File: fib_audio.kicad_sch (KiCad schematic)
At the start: 58 parts, among them J701 DNP AUDIO-JACK-8P-SMD, J702 SPK_JST_L, J703 SPK_JST_R, K701 BUTTON-4PDTSM-62K-S-V-T/R(SN4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, U701 WM8960CGEFL, X701 24MHz 306020014

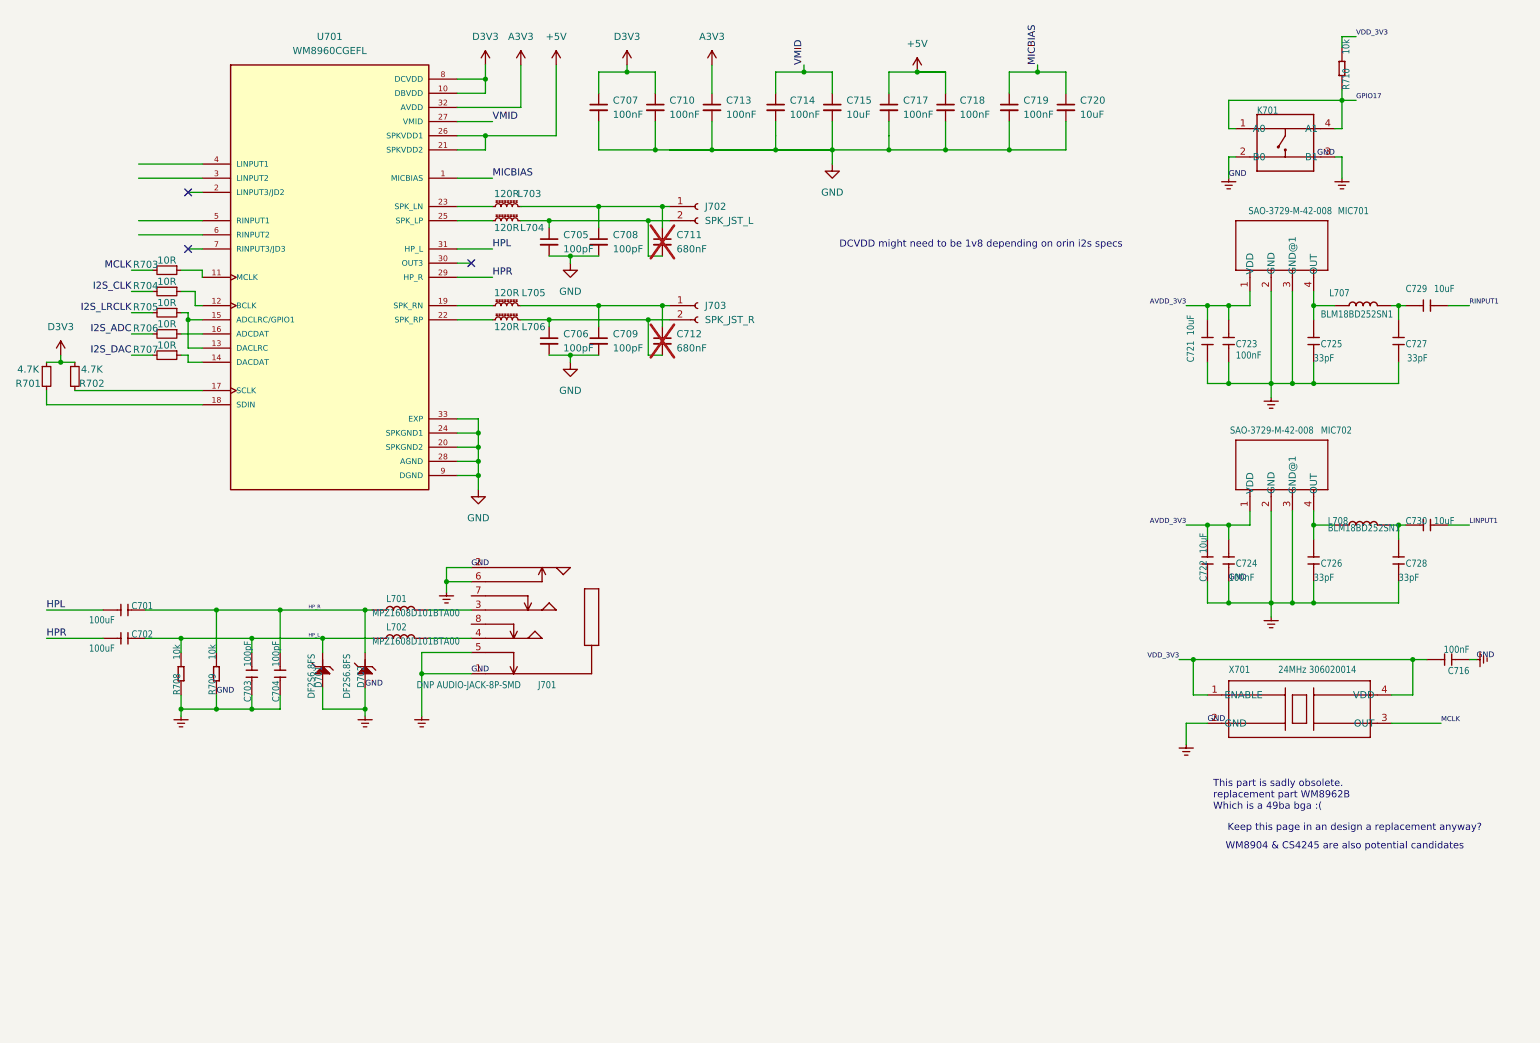
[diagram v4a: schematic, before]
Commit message: added all missing footprints, fixed library & footprint links, did layout out 99% of components, all that's left is rtc(?), peripherals, routing & lengthmatching and final sanity checks
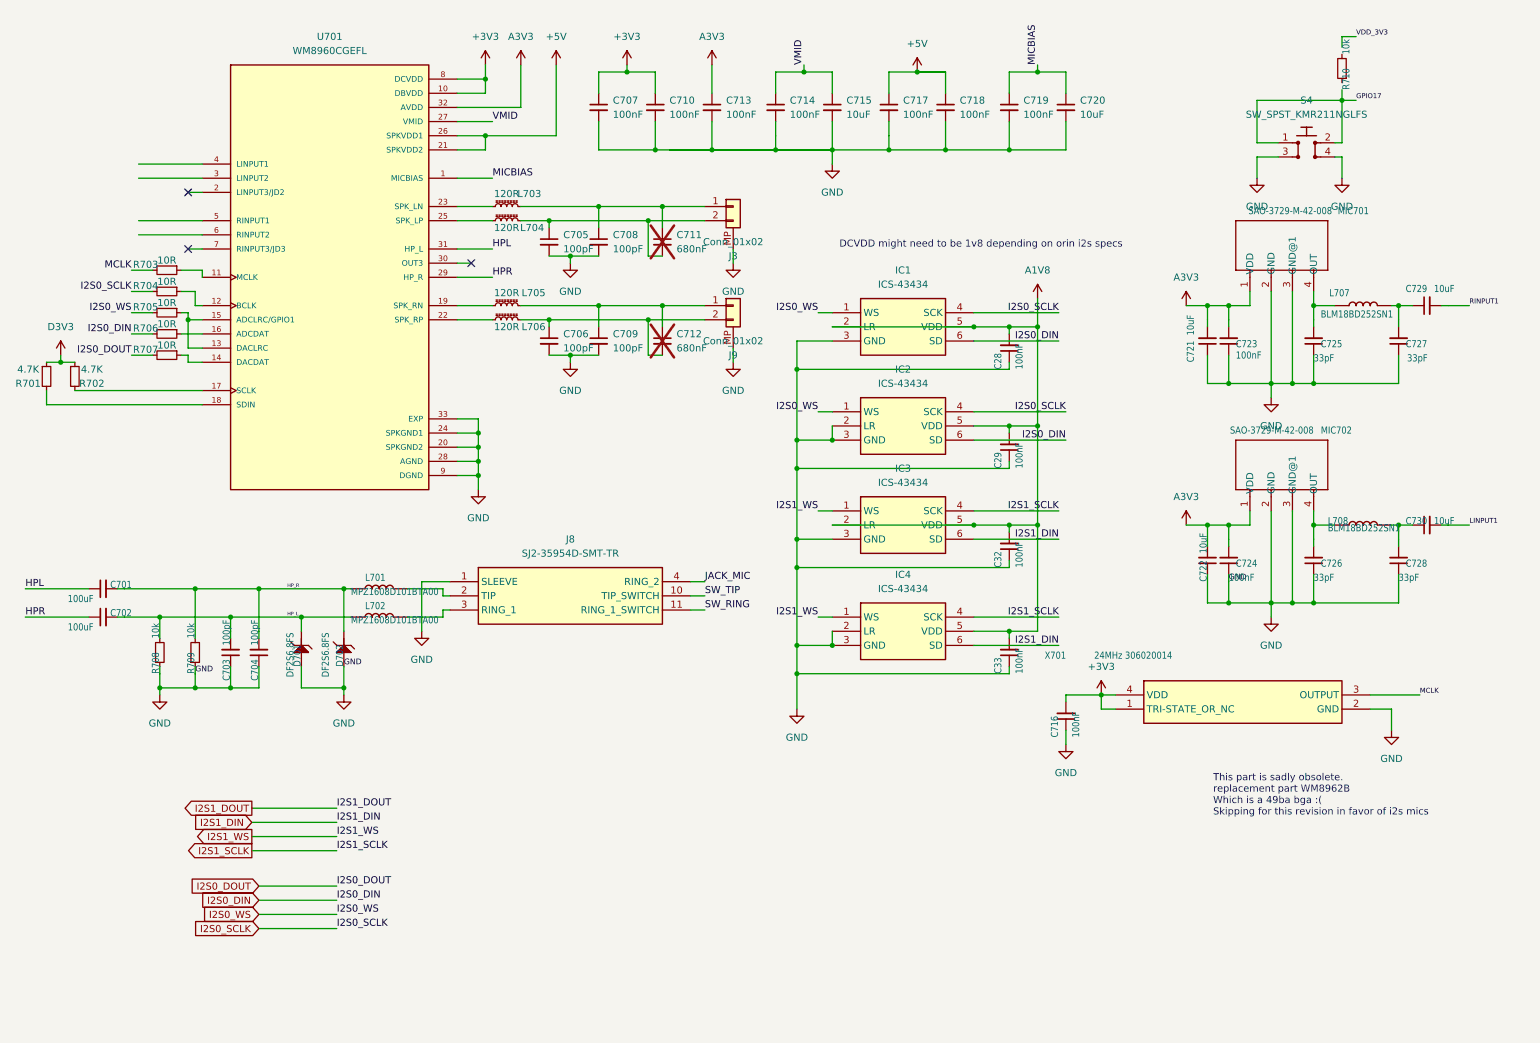
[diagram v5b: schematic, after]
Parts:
- removed J701: DNP AUDIO-JACK-8P-SMD, Untitled:AUDIO8P-SMD-3.5-14.5X6.1X4.0MM, symbol Untitled-eagle-import:AUDIO-JACK-8P-SMD'PJ-393'
- removed J702: SPK_JST_L, Capacitor_SMD:C_0603_1608Metric, symbol Connector:Conn_01x02_Socket
- removed J703: SPK_JST_R, Capacitor_SMD:C_0603_1608Metric, symbol Connector:Conn_01x02_Socket
- removed K701: BUTTON-4PDTSM-62K-S-V-T/R(SN431), Untitled:SW4-SMD-6.0X6.0X5.0MM, symbol Untitled-eagle-import:BUTTON-4PDTSM-62K-S-V-T/R(SN431)
- added C28, C29, C32, C33: 100nF, Capacitor_SMD:C_0402_1005Metric, symbol Fibel2:C_Small_Rota
- added IC1, IC2, IC3, IC4: ICS-43434, ICS43434, symbol Fibel2:ICS-43434
- added J3, J9: Conn_01x02, Connector_JST:JST_PH_S2B-PH-SM4-TB_1x02-1MP_P2.00mm_Horizontal, symbol Fibel2:JST_2_SMD
- added J8: SJ2-35954D-SMT-TR, SJ235954DSMTTR, symbol Fibel2:SJ2-35954D-SMT-TR
- added S4: SW_SPST_KMR211NGLFS, Fibel2:KMR211NGLFS, symbol Fibel2:SW_KMR211NGLFS_SMD
- C701, C702: symbol Untitled-eagle-import:CAP-0805 -> Fibel2:C_Small_Rota
- C703, C704, C716, C723, C724, C725, C726, C727, C728: symbol Untitled-eagle-import:CAP-0402 -> Fibel2:C_Small_Rota
- C721, C722, C729, C730: symbol Untitled-eagle-import:CAP-0603 -> Fibel2:C_Small_Rota
- D701, D702: symbol Untitled-eagle-import:D-ESD-2P'DF2S6.8FS' -> Fibel2:D-ESD-2P'DF2S6.8FS'
- L701, L702, L707, L708: symbol Untitled-eagle-import:INDUCTOR/FERRITE-BEAD'0603' -> Fibel2:INDUCTOR/FERRITE-BEAD'0603'
- MIC701, MIC702: footprint Untitled:MIC4-SMD-3.76X2.95MM -> Fibel2:MIC_Respeaker; symbol Untitled-eagle-import:MIC-MSM421A3729H8-C -> Fibel2:MIC-MSM421A3729H8-C
- R708, R709, R710: symbol Untitled-eagle-import:Discrete-new_RES-0402 -> Fibel2:R_Small_Rota
- X701: footprint Untitled:OSC4-SMD-2.5X2.0X0.8MM -> Fibel2:ECS2520MV; symbol Untitled-eagle-import:CRYSTAL-OSCILLATOR2.52.0 -> Fibel2:ECS-327ATQ2520MV-24M; Height (none) -> 0.9; Manufacturer_Name (none) -> ECS; Manufacturer_Part_Number (none) -> ECS-327ATQ2520MV-BS-TR; Mouser Part Number (none) -> 520-327ATQ2520MVBSTR; Mouser Price/Stock (none) -> https://www.mouser.co.uk/ProductDetail/ECS/ECS-327ATQ2520MV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
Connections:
- net AVDD_3V3 is gone; now on net A3V3: C721.2, C722.2, C723.2, C724.2, MIC701.1 (VDD), MIC702.1 (VDD)
- net D3V3: no longer C707.1, C710.1, U701.10 (DBVDD), U701.8 (DCVDD)
- net GND: now also C28.1, C29.1, C32.1, C33.1, IC1.3 (GND), IC2.2 (LR), IC2.3 (GND), IC3.3 (GND), IC4.2 (LR), IC4.3 (GND), J3.MP, J8.1 (SLEEVE), J9.MP, S4.3, S4.4
- net GPIO17: now also S4.1, S4.2; no longer R710.1
- net VDD_3V3: no longer C716.2, R710.2, X701.1 (ENABLE), X701.4 (VDD)
- net at C709.1, C712.1, L705.2: now also J9.1 (Pin_1)
- net at C706.1, C712.2, L706.2: now also J9.2 (Pin_2)
- net at C705.1, C711.2, L704.2: now also J3.2 (Pin_2)
- net at L701.2: now also J8.2 (TIP)
- net at L702.2: now also J8.3 (RING_1)
- net at C708.1, C711.1, L703.2: now also J3.1 (Pin_1)
- net I2S_ADC renamed I2S0_DIN
- net I2S0_DIN: now also IC1.6 (SD), IC2.6 (SD)
- net I2S_CLK renamed I2S0_SCLK
- net I2S0_SCLK: now also IC1.4 (SCK), IC2.4 (SCK)
- net I2S_DAC renamed I2S0_DOUT
- net I2S_LRCLK renamed I2S0_WS
- net I2S0_WS: now also IC1.1 (WS), IC2.1 (WS)
- new net +3V3: C707.1, C710.1, C716.2, U701.10 (DBVDD), U701.8 (DCVDD), X701.1 (TRI-STATE_OR_NC), X701.4 (VDD)
- new net A1V8: C28.2, C29.2, C32.2, C33.2, IC1.2 (LR), IC1.5 (VDD), IC2.5 (VDD), IC3.2 (LR), IC3.5 (VDD), IC4.5 (VDD)
- new net I2S1_DIN: IC3.6 (SD), IC4.6 (SD)
- new net I2S1_SCLK: IC3.4 (SCK), IC4.4 (SCK)
- new net I2S1_WS: IC3.1 (WS), IC4.1 (WS)
- new net JACK_MIC: J8.4 (RING_2)
- new net SW_RING: J8.11 (RING_1_SWITCH)
- new net SW_TIP: J8.10 (TIP_SWITCH)
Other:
- note added: "This part is sadly obsolete. replacement part WM8962B Which is a 49ba bga :( Skipping for this revision in favor of i2s mics"
- note removed: "Keep this page in an design a replacement anyway?"
- note removed: "This part is sadly obsolete. replacement part WM8962B Which is a 49ba bga :("
- note removed: "WM8904 & CS4245 are also potential candidates"
- moved on the sheet: D701, D702, L701, L702

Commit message: did length tuning, routing of final submodules and most of power routing
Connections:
- net D3V3 is gone; now on net +3V3: R701.1, R702.1
- net GPIO17 is gone; now on an unnamed net: S4.1, S4.2
- net LINPUT1: now also U701.4 (LINPUT1)
- net RINPUT1: now also U701.5 (RINPUT1)
- net VDD_3V3: now also R710.2
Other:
- moved on the sheet: R710
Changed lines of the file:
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@@
 	)
 	(junction
-		(at 254 27.94)
-		(diameter 0)
-		(color 0 0 0 0)
-	)
-	(junction
 		(at 54.61 120.65)
 		(diameter 0)
@@
 	)
 	(junction
+		(at 254 27.94)
+		(diameter 0)
+		(color 0 0 0 0)
+	)
+	(junction
 		(at 46.99 67.31)
 		(diameter 0)
@@
 	(wire
 		(pts
-			(xy 254 18.415) (xy 254 16.51)
-		)
-		(stroke
-			(width 0.1524)
-			(type solid)
-		)
-	)
-	(wire
-		(pts
 			(xy 156.21 93.98) (xy 156.21 106.68)
 		)
@@
 	(wire
 		(pts
-			(xy 254 27.94) (xy 254 35.56)
-		)
-		(stroke
-			(width 0)
-			(type default)
-		)
-	)
-	(wire
-		(pts
 			(xy 36.83 58.42) (xy 40.64 58.42)
 		)
@@
 	(wire
 		(pts
+			(xy 254 26.67) (xy 254 27.94)
+		)
+		(stroke
+			(width 0.1524)
+			(type solid)
+		)
+	)
+	(wire
+		(pts
 			(xy 144.78 74.93) (xy 144.78 72.39)
 		)
@@
 	(wire
 		(pts
-			(xy 254 27.94) (xy 256.54 27.94)
-		)
-		(stroke
-			(width 0.1524)
-			(type solid)
-		)
-	)
-	(wire
-		(pts
 			(xy 54.61 123.19) (xy 54.61 120.65)
 		)
@@
 	(wire
 		(pts
-			(xy 254 27.94) (xy 254 26.035)
-		)
-		(stroke
-			(width 0.1524)
-			(type solid)
-		)
-	)
-	(wire
-		(pts
 			(xy 187.96 125.73) (xy 203.2 125.73)
 		)
@@
 	(wire
 		(pts
+			(xy 254 16.51) (xy 254 17.78)
+		)
+		(stroke
+			(width 0.1524)
+			(type solid)
+		)
+	)
+	(wire
+		(pts
 			(xy 48.26 115.57) (xy 48.26 124.46)
 		)
@@
 	(wire
 		(pts
+			(xy 254 27.94) (xy 254 35.56)
+		)
+		(stroke
+			(width 0.1524)
+			(type solid)
+		)
+	)
+	(wire
+		(pts
 			(xy 140.97 31.75) (xy 140.97 36.83)
 		)
@@
 	(wire
 		(pts
+			(xy 254 19.05) (xy 254 17.78)
+		)
+		(stroke
+			(width 0)
+			(type default)
+		)
+	)
+	(wire
+		(pts
 			(xy 95.25 57.15) (xy 97.79 57.15)
 		)
@@
 	(wire
 		(pts
+			(xy 254 24.13) (xy 254 26.67)
+		)
+		(stroke
+			(width 0)
+			(type default)
+		)
+	)
+	(wire
+		(pts
 			(xy 199.39 68.58) (xy 199.39 86.36)
 		)
@@
 		)
 	)
+	(label "RINPUT1"
+		(at 38.1 49.53 0)
+		(fields_autoplaced yes)
+		(effects
+			(font
+				(size 0.889 0.889)
+			)
+			(justify left bottom)
+		)
+	)
 	(label "I2S0_WS"
 		(at 73.66 173.99 0)
@@
 		)
 	)
-	(label "GPIO17"
-		(at 256.54 27.94 0)
+	(label "LINPUT1"
+		(at 38.1 39.37 0)
 		(fields_autoplaced yes)
 		(effects
@@
 	(symbol
 		(lib_id "Fibel2:R_Small_Rota")
-		(at 254 22.225 270)
+		(at 254 21.59 270)
 		(mirror x)
 		(unit 1)
@@
 		(dnp no)
 		(property "Reference" "R710"
-			(at 254 26.035 0)
+			(at 256.032 24.765 0)
 			(effects
 				(font
@@
 		)
 		(property "Value" "10k"
-			(at 254 19.685 0)
+			(at 254 19.05 0)
 			(effects
 				(font
@@
 		)
 		(property "Footprint" "Resistor_SMD:R_0402_1005Metric"
-			(at 254 22.225 0)
+			(at 254 21.59 0)
 			(effects
 				(font
@@
 		)
 		(property "Datasheet" "~"
-			(at 254 22.225 0)
+			(at 254 21.59 0)
 			(effects
 				(font
@@
 		)
 		(property "Description" "Resistor, small symbol"
-			(at 254 22.225 0)
+			(at 254 21.59 0)
 			(effects
 				(font
@@
 			)
 		)
-		(property "Value" "D3V3"
+		(property "Value" "+3V3"
 			(at 24.13 68.58 0)
 			(effects

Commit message: added port expander and level shifters, routed peripherals fixed most drc errors, assigned gpios etc.
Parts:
- IC1, IC2, IC3, IC4: footprint ICS43434 -> Fibel2:ICS43434
- J8: footprint SJ235954DSMTTR -> Fibel2:SJ235954DSMTTR
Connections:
- net +3V3: no longer C707.1, C710.1, U701.10 (DBVDD), U701.8 (DCVDD)
- net A1V8 renamed +1V8
- net +1V8: now also C707.1, C710.1, U701.10 (DBVDD), U701.8 (DCVDD)
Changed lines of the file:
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@@
 			)
 		)
-		(property "Footprint" "SJ235954DSMTTR"
+		(property "Footprint" "Fibel2:SJ235954DSMTTR"
 			(at 133.35 209.22 0)
 			(effects
@@
 			)
 		)
-		(property "Footprint" "ICS43434"
+		(property "Footprint" "Fibel2:ICS43434"
 			(at 184.15 160.96 0)
 			(effects
@@
 			)
 		)
-		(property "Value" "+3V3"
+		(property "Value" "+1V8"
 			(at 125.73 16.51 0)
 			(effects
@@
 			)
 		)
-		(property "Footprint" "ICS43434"
+		(property "Footprint" "Fibel2:ICS43434"
 			(at 184.15 215.57 0)
 			(effects
@@
 			)
 		)
-		(property "Footprint" "ICS43434"
+		(property "Footprint" "Fibel2:ICS43434"
 			(at 184.15 196.52 0)
 			(effects
@@
 			)
 		)
-		(property "Value" "+3V3"
+		(property "Value" "+1V8"
 			(at 100.33 16.51 0)
 			(effects
@@
 			)
 		)
-		(property "Value" "A1V8"
+		(property "Value" "+1V8"
 			(at 199.39 58.42 0)
 			(effects
@@
 			)
 		)
-		(property "Footprint" "ICS43434"
+		(property "Footprint" "Fibel2:ICS43434"
 			(at 184.15 178.74 0)
 			(effects

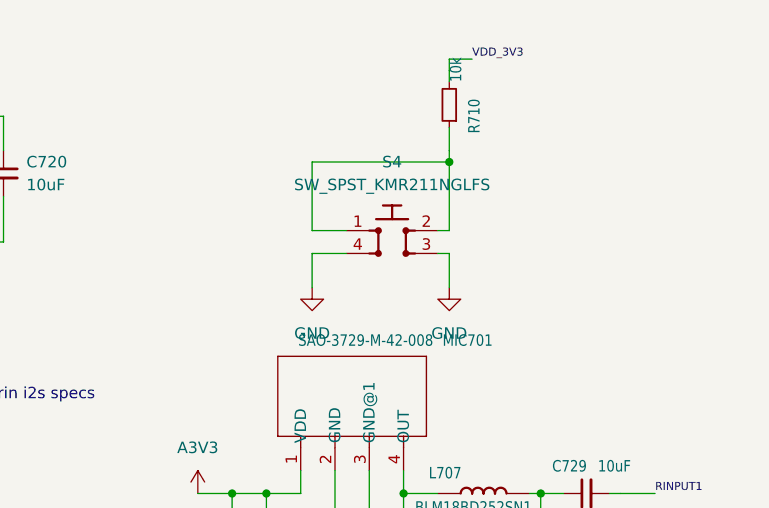
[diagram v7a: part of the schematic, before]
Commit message: routed epd displays, added testpoints and all the little checks and fixe, (regrettably) removed the i80 connector, 99% there, need to double check some things add peripheral connectors, shared-ish storage and vias vias vias
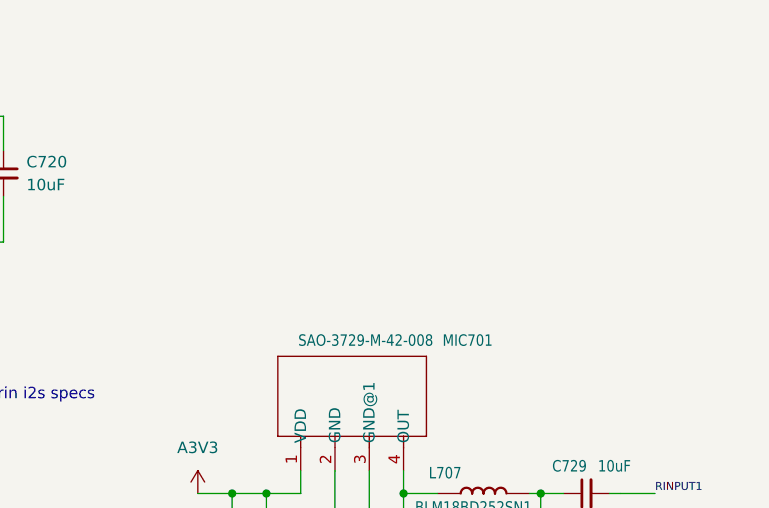
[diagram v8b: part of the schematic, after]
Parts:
- removed R710: 10k, Resistor_SMD:R_0402_1005Metric, symbol Fibel2:R_Small_Rota
- removed S4: SW_SPST_KMR211NGLFS, Fibel2:KMR211NGLFS, symbol Fibel2:SW_KMR211NGLFS_SMD
